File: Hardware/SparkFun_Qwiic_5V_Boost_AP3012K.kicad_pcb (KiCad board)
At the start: 2 copper layers, 25.4 x 25.4 mm, 67 parts, among them J1 Qwiic_RA, J2 Qwiic_RA, J3 Conn_01x06, Q1 BSS138, Q2 BSS138, U5 AP3012

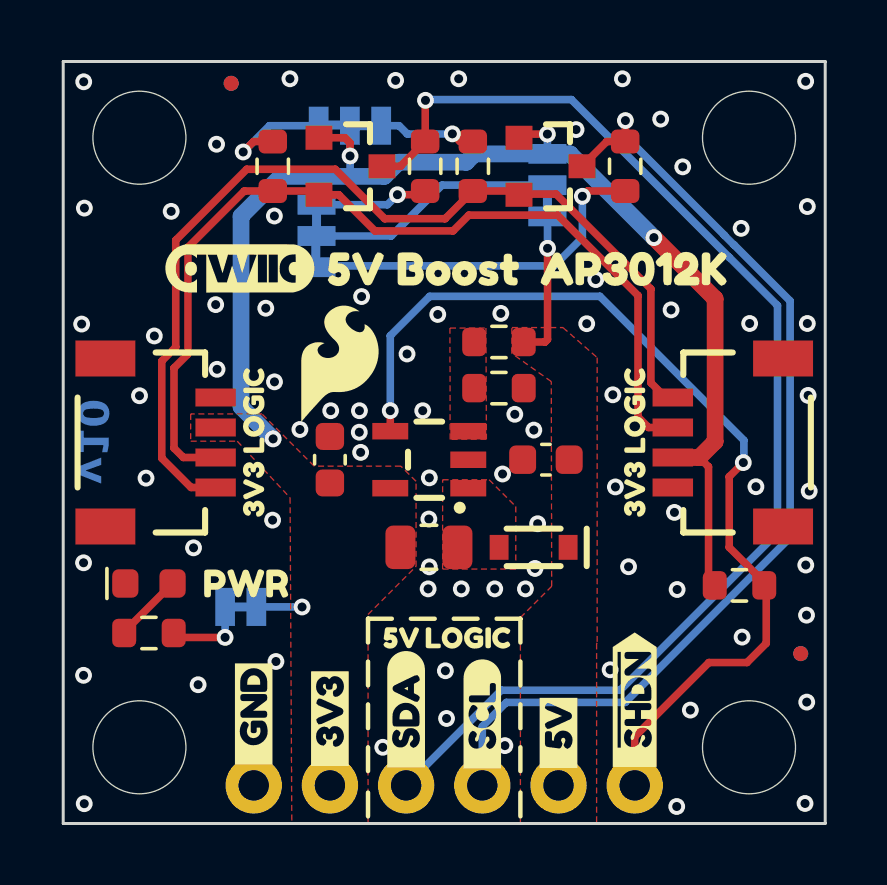
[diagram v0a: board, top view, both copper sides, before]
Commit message: added 2 test points
-added test points for 3V3 logic level SDA/SCL
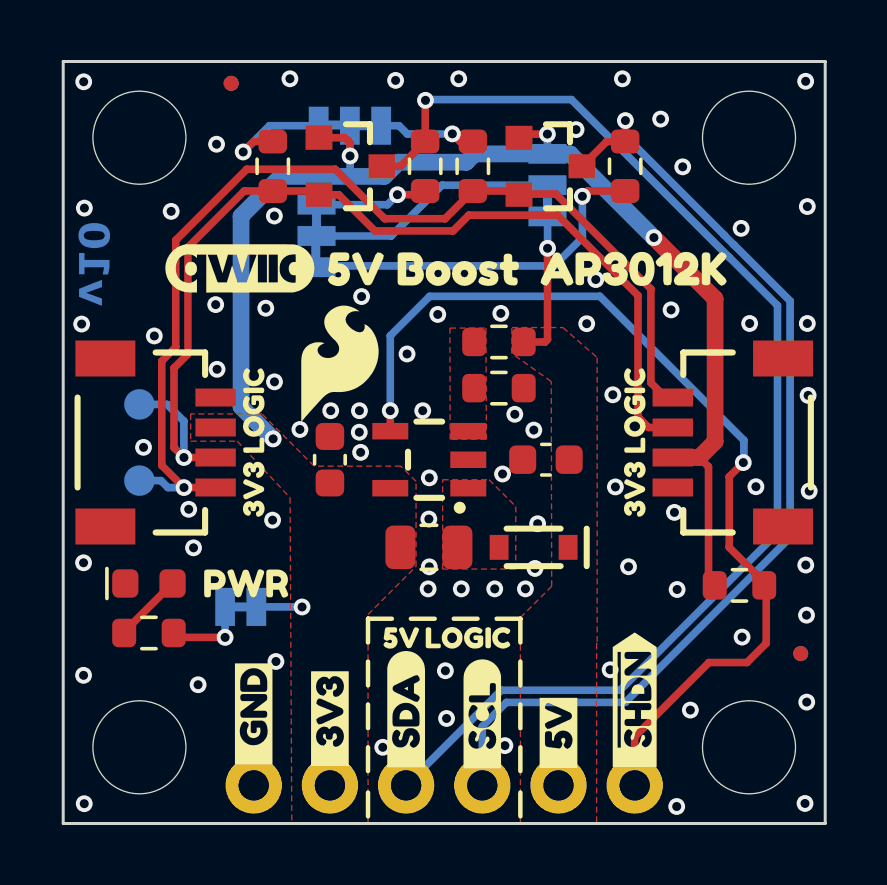
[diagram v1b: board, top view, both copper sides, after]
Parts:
- added TP1: 1.0mm, SparkFun-Connector:TestPoint-1.0mm, B.Cu at (125.8, 96.8)
- added TP2: 1.0mm, SparkFun-Connector:TestPoint-1.0mm, B.Cu at (125.8, 99.4)
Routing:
- net SDA: track 31.5 -> 34.5 mm, vias 0 -> 1
- net SCL: track 33.1 -> 34.8 mm, vias 0 -> 1
